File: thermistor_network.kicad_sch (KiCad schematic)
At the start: 1 part

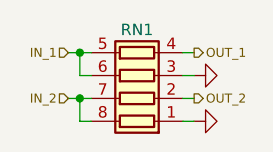
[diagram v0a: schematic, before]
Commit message: schematic: Add board interconnect connectors
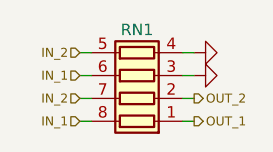
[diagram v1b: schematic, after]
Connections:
- net GND: now also RN1.4 (R4.1); no longer RN1.1 (R1.1)
- net IN_1: now also RN1.8 (R1.2); no longer RN1.5 (R4.2)
- net IN_2: now also RN1.5 (R4.2); no longer RN1.8 (R1.2)
- net OUT_1: now also RN1.1 (R1.1); no longer RN1.4 (R4.1)
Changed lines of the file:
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@@
 		(company "York Formula Student")
-	)
-	(junction
-		(at 106.68 52.07)
-		(diameter 0)
-		(color 0 0 0 0)
-	)
-	(junction
-		(at 106.68 46.99)
-		(diameter 0)
-		(color 0 0 0 0)
-	)
-	(wire
-		(pts
-			(xy 106.68 49.53) (xy 106.68 46.99)
-		)
-		(stroke
-			(width 0)
-			(type default)
-		)
 	)
 	(wire
@@
 	(wire
 		(pts
-			(xy 105.41 46.99) (xy 106.68 46.99)
+			(xy 106.68 52.07) (xy 107.95 52.07)
 		)
 		(stroke
@@
 	(wire
 		(pts
-			(xy 106.68 54.61) (xy 106.68 52.07)
-		)
-		(stroke
-			(width 0)
-			(type default)
-		)
-	)
-	(wire
-		(pts
 			(xy 107.95 54.61) (xy 106.68 54.61)
 		)
@@
 	(wire
 		(pts
-			(xy 105.41 52.07) (xy 106.68 52.07)
-		)
-		(stroke
-			(width 0)
-			(type default)
-		)
-	)
-	(wire
-		(pts
-			(xy 107.95 49.53) (xy 106.68 49.53)
-		)
-		(stroke
-			(width 0)
-			(type default)
-		)
-	)
-	(wire
-		(pts
-			(xy 106.68 52.07) (xy 107.95 52.07)
+			(xy 106.68 49.53) (xy 107.95 49.53)
 		)
 		(stroke
@@
 	(hierarchical_label "OUT_1"
 		(shape output)
-		(at 119.38 46.99 0)
+		(at 119.38 54.61 0)
 		(effects
 			(font
@@
 	(hierarchical_label "IN_2"
 		(shape input)
-		(at 105.41 52.07 180)
+		(at 106.68 52.07 180)
 		(effects
 			(font
@@
 		)
 	)
+	(hierarchical_label "IN_2"
+		(shape input)
+		(at 106.68 46.99 180)
+		(effects
+			(font
+				(size 1 1)
+			)
+			(justify right)
+		)
+	)
 	(hierarchical_label "IN_1"
 		(shape input)
-		(at 105.41 46.99 180)
+		(at 106.68 54.61 180)
+		(effects
+			(font
+				(size 1 1)
+			)
+			(justify right)
+		)
+	)
+	(hierarchical_label "IN_1"
+		(shape input)
+		(at 106.68 49.53 180)
 		(effects
 			(font
@@
 	(symbol
 		(lib_id "power:GND")
-		(at 119.38 54.61 90)
+		(at 119.38 46.99 90)
 		(unit 1)
 		(exclude_from_sim no)
@@
 		(fields_autoplaced yes)
 		(property "Reference" "#PWR072"
-			(at 125.73 54.61 0)
+			(at 125.73 46.99 0)
 			(effects
 				(font
@@
 		)
 		(property "Value" "GND"
-			(at 124.46 54.61 0)
+			(at 124.46 46.99 0)
 			(effects
 				(font
@@
 		)
 		(property "Footprint" ""
-			(at 119.38 54.61 0)
+			(at 119.38 46.99 0)
 			(effects
 				(font
@@
 		)
 		(property "Datasheet" ""
-			(at 119.38 54.61 0)
+			(at 119.38 46.99 0)
 			(effects
 				(font
@@
 		)
 		(property "Description" "Power symbol creates a global label with name \"GND\" , ground"
-			(at 119.38 54.61 0)
+			(at 119.38 46.99 0)
 			(effects
 				(font

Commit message: *: Minor cleanup
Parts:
- RN1: value R_Pack04 -> 1k
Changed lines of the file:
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@@
 			)
 		)
-		(property "Value" "R_Pack04"
+		(property "Value" "1k"
 			(at 113.03 43.18 90)
 			(effects

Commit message: *: Rework BOM
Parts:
- RN1: value 1k -> 10k; DigiKey # (none) -> CAY16-103J4LFCT-ND; LCSC # (none) -> C784821; Mfr (none) -> Bourns; Mfr # (none) -> CAY16-103J4LF; Mouser # (none) -> 652-CAY16-103J4LF
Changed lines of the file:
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@@
 			)
 		)
-		(property "Value" "1k"
+		(property "Value" "10k"
 			(at 113.03 43.18 90)
 			(effects
@@
 			(effects
 				(font
+					(size 1.27 1.27)
+				)
+				(hide yes)
+			)
+		)
+		(property "DigiKey #" "CAY16-103J4LFCT-ND"
+			(at 113.03 49.53 90)
+			(effects
+				(font
+					(size 1.27 1.27)
+				)
+				(hide yes)
+			)
+		)
+		(property "LCSC #" "C784821"
+			(at 113.03 49.53 90)
+			(effects
+				(font
+					(size 1.27 1.27)
+				)
+				(hide yes)
+			)
+		)
+		(property "Mouser #" "652-CAY16-103J4LF"
+			(at 113.03 49.53 90)
+			(effects
+				(font
+					(size 1.27 1.27)
+				)
+				(hide yes)
+			)
+		)
+		(property "Mfr" "Bourns"
+			(at 113.03 49.53 90)
+			(effects
+				(font
+					(size 1.27 1.27)
+				)
+				(hide yes)
+			)
+		)
+		(property "Mfr #" "CAY16-103J4LF"
+			(at 113.03 49.53 90)
+			(effects
+				(font

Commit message: schematic: Cleanup BOM
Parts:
- RN1: DigiKey # CAY16-103J4LFCT-ND -> 13-YC324-FK-0710KLCT-ND; LCSC # C784821 -> C876914; Mfr Bourns -> YAGEO; Mfr # CAY16-103J4LF -> YC324-FK-0710KL; Mouser # 652-CAY16-103J4LF -> 603-YC324-FK-0710KL
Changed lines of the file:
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@@
 			)
 		)
-		(property "DigiKey #" "CAY16-103J4LFCT-ND"
+		(property "DigiKey #" "13-YC324-FK-0710KLCT-ND"
 			(at 113.03 49.53 90)
 			(effects
@@
 			)
 		)
-		(property "LCSC #" "C784821"
+		(property "LCSC #" "C876914"
 			(at 113.03 49.53 90)
 			(effects
@@
 			)
 		)
-		(property "Mouser #" "652-CAY16-103J4LF"
+		(property "Mouser #" "603-YC324-FK-0710KL"
 			(at 113.03 49.53 90)
 			(effects
@@
 			)
 		)
-		(property "Mfr" "Bourns"
+		(property "Mfr" "YAGEO"
 			(at 113.03 49.53 90)
 			(effects
@@
 			)
 		)
-		(property "Mfr #" "CAY16-103J4LF"
+		(property "Mfr #" "YC324-FK-0710KL"
 			(at 113.03 49.53 90)
 			(effects
